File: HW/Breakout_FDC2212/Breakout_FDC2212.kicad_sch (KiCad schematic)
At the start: 21 parts, among them J1 SM04B-SRSS-TB, J2 Conn_01x02, J3 Conn_01x02, J4 Conn_01x06, U5 625L3C040M00000, U6 FDC2212

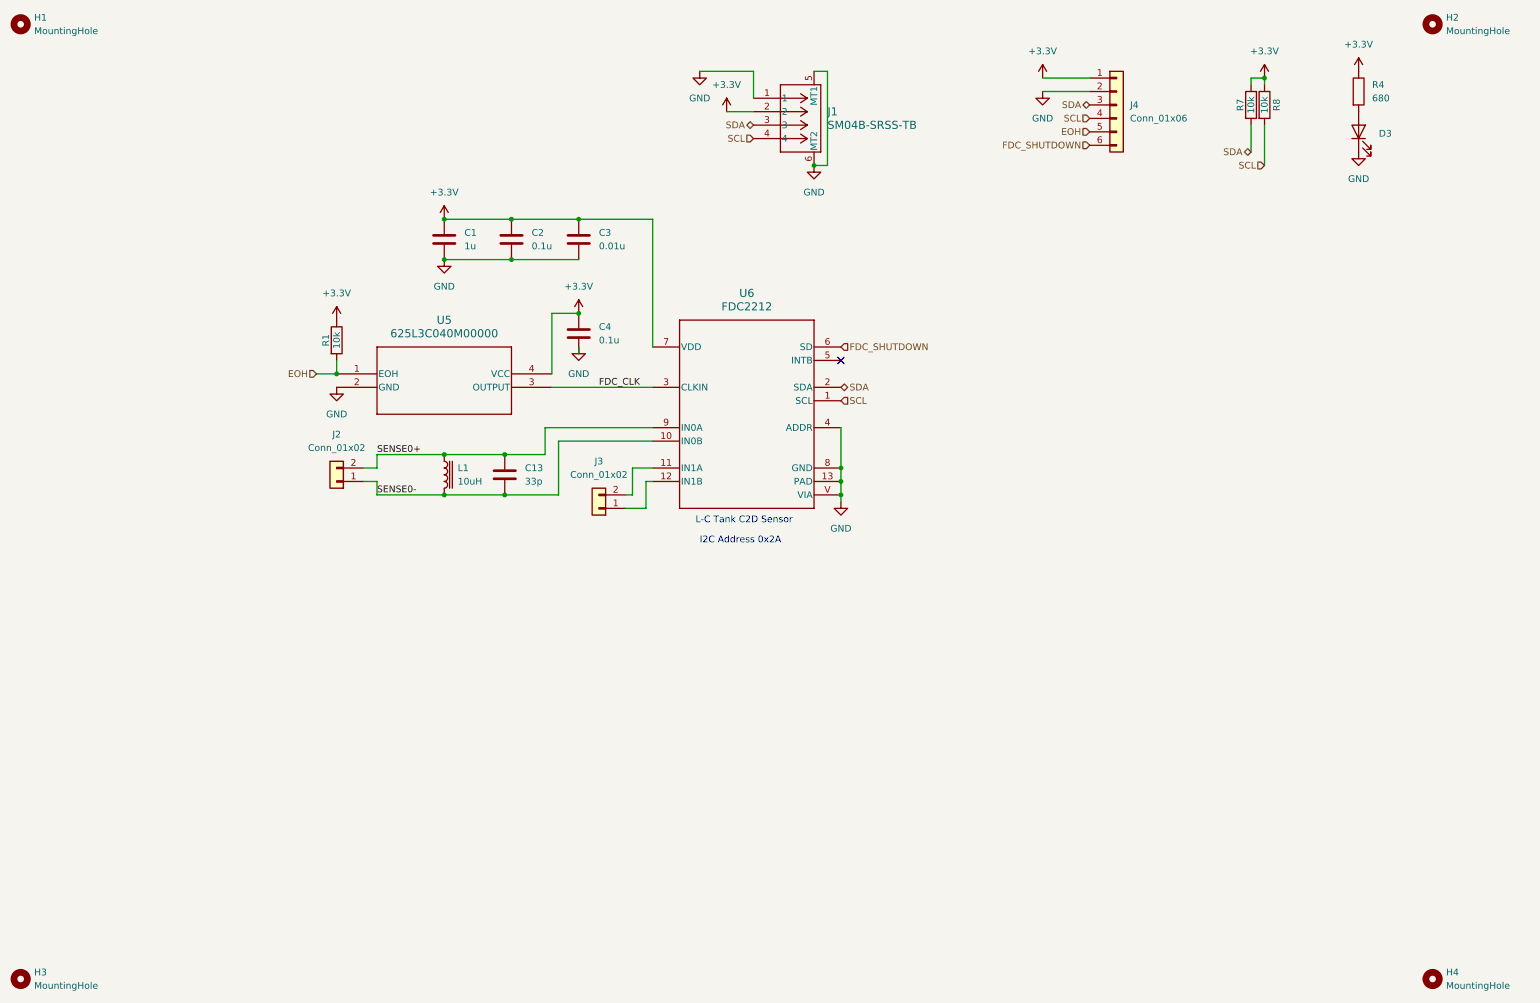
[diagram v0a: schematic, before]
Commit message: Align pin holes for potential breadboard mounting
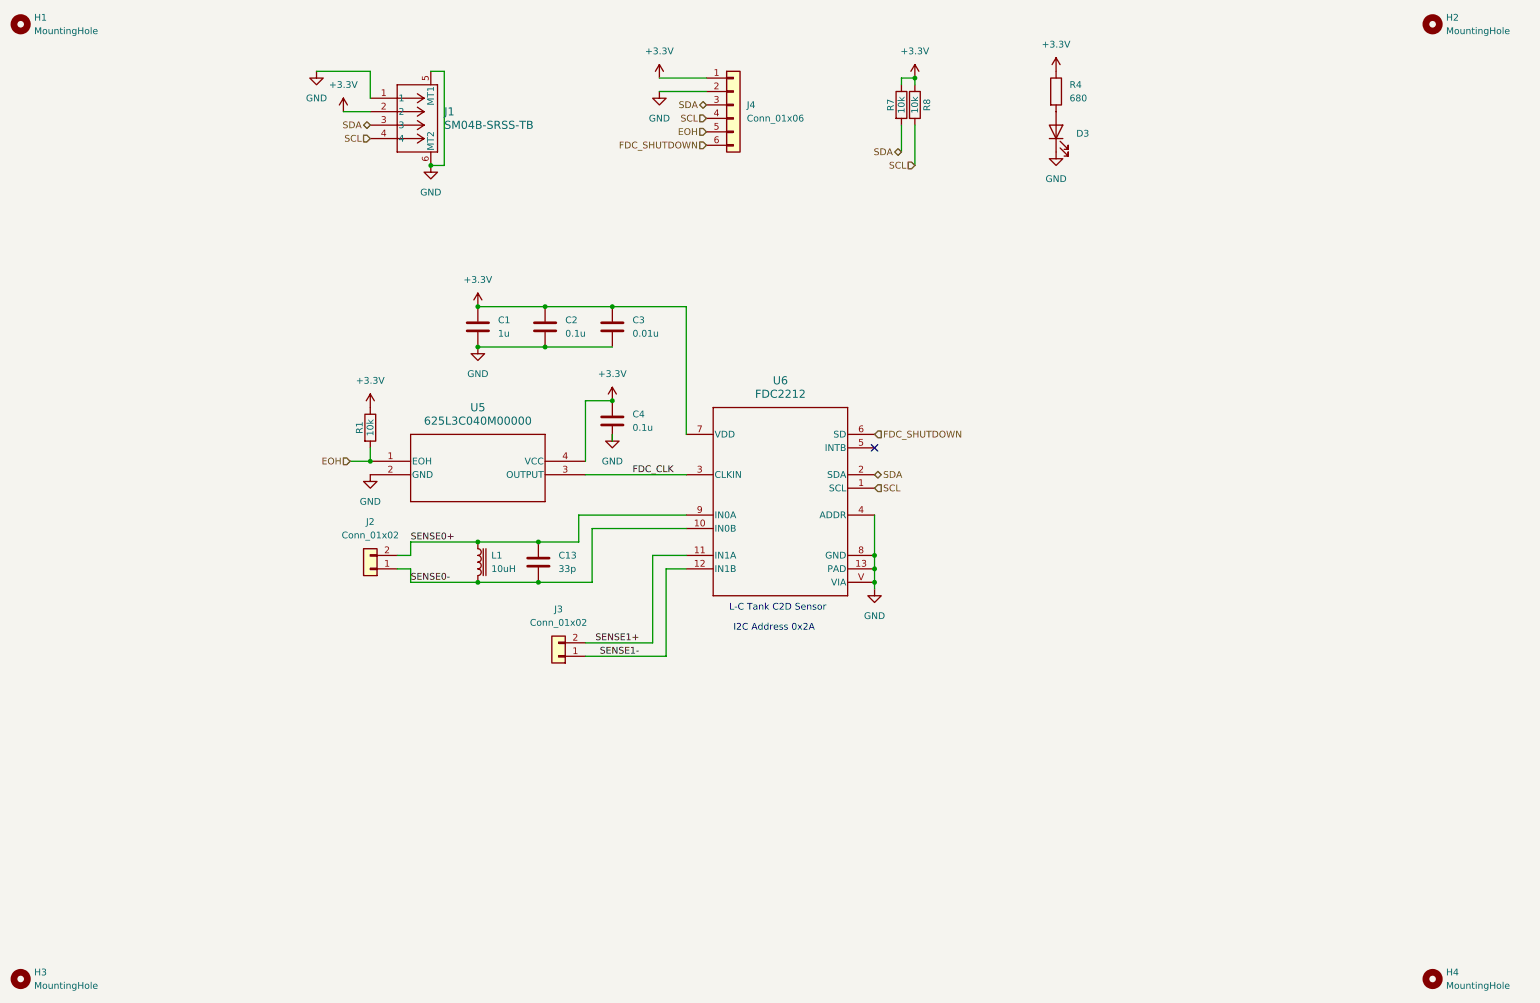
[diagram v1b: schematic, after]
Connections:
- net SENSE1+: now reaches J3.2 (Pin_2), U6.11 (IN1A)
- net SENSE1-: now reaches J3.1 (Pin_1), U6.12 (IN1B)
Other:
- moved on the sheet: C1, C13, C2, C3, C4, D3, J1, J2, J3, J4, L1, R1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
